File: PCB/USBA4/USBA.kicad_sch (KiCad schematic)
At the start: 23 parts, among them J1 USB_A, J2 Shelly, U2 ESP32-S3-MINI-1, U5 MD8942, U7 SHT40

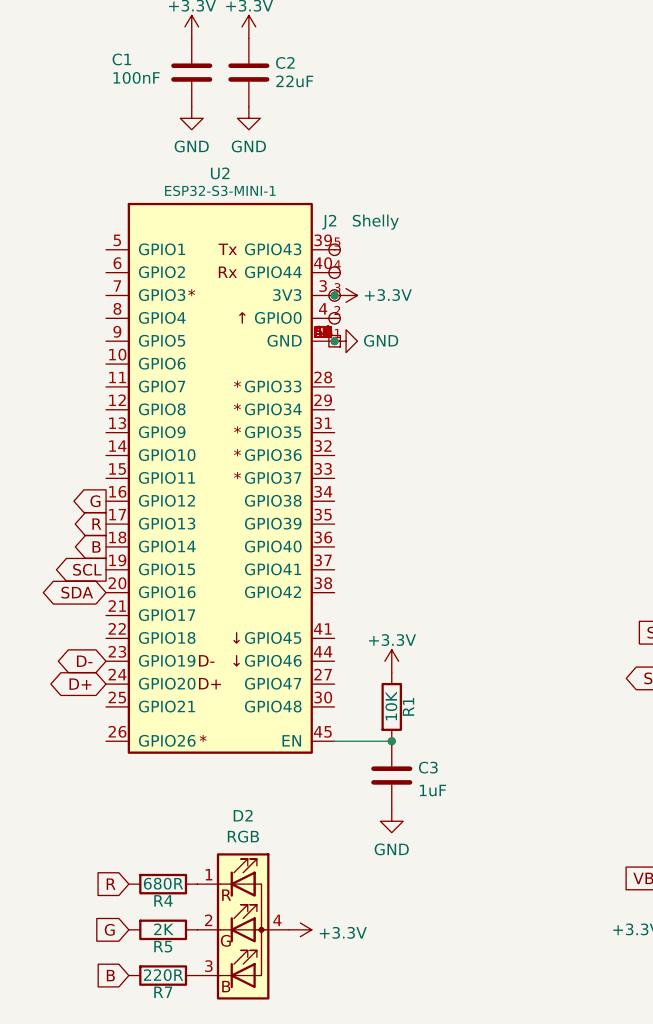
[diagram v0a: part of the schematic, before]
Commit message: Tidy, fix GND, and add tear drops
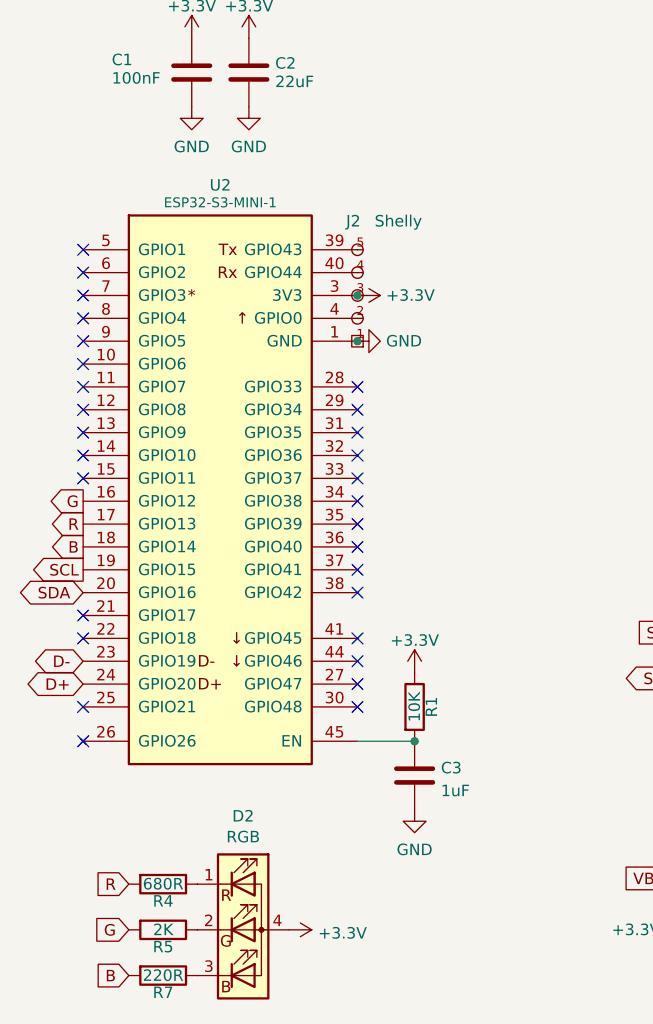
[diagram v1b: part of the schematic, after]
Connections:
- net GND: now also U2.59 (GND), U2.62 (GND), U2.63 (GND), U2.64 (GND)
- no-connect marks 1 -> 30
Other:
- moved on the sheet: C3, J2, R1
